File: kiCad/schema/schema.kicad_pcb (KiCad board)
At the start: 2 copper layers, 90 x 127.1 mm, 30 parts, among them J1 Conn_01x06_Pin, J11 Switch, J14 Conn_01x06_Pin, J15 MOSFET, J2 Esp32, J3 M1 Right, J4 M2 Left, J5 Bat, J6 Buck, Q1 Q_Photo_NPN, Q2 Q_Photo_NPN, Q3 Q_Photo_NPN, Q4 Q_Photo_NPN

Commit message: Day 17 - PCB 60% Done
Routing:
- net /ENC B2: track 0.00 -> 41.4 mm
- net /3V3: track 0.00 -> 37.4 mm
- net /ENC A1: track 0.00 -> 34.7 mm
- net /ENC A2: track 0.00 -> 33.2 mm, vias 0 -> 1
- net /ENC B1: track 0.00 -> 29.8 mm
- net /BIN 2: track 0.00 -> 26.6 mm, vias 0 -> 2
- net /BIN 1: track 0.00 -> 23.2 mm, vias 0 -> 2
- net /AIN 2: track 0.00 -> 19.5 mm, vias 0 -> 2
- net /AIN 1: track 0.00 -> 18.6 mm, vias 0 -> 2
- net /BUCK +: track 71.8 -> 73.0 mm
- added copper zone on B.Cu, net /GND
- added copper zone on F.Cu, net /GND

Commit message: Day 19 - PCB done
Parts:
- C1 100nF: renamed from C1
- C2 47 µF: renamed from C2
- C3 100nF: renamed from C3
- R1 120 : renamed from R1
- R10 10k: renamed from R10
- R2 120: renamed from R2
- R3 120: renamed from R3
- R4 120: renamed from R4
- R7 10k : renamed from R7
- R8 10k: renamed from R8
- R9 10k: renamed from R9
- moved C1 100nF 53.7 mm to (76.7, 108.7), turned to 90 degrees
- moved C2 47 µF 50.7 mm to (81.0, 106.7), turned to -90 degrees
- moved D3 2.85 mm to (109.9, 38.7)
- moved D4 2.14 mm to (130.1, 51.4)
- moved Q4 2.06 mm to (136.3, 57.6)
- moved R3 120 1.80 mm to (116.3, 56.6)
- moved R9 10k 1.80 mm to (121.4, 56.4)
- moved R2 120 1.27 mm to (88.4, 56.4)
- moved R8 10k 1.27 mm to (92.7, 56.6)
- moved J15 1.12 mm to (103.9, 53.1)
- moved J3 0.76 mm to (84.8, 111.5)
- moved J4 0.76 mm to (119.9, 111.5)
- moved D2 0.59 mm to (82.0, 38.7)
- moved Q3 0.31 mm to (120.3, 38.7)
- moved Q2 0.20 mm to (92.4, 38.7)
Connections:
- C1 100nF pad 1: /GND -> /BUCK +
- C1 100nF pad 2: /BUCK + -> /GND
- C2 47 µF pad 1: /BUCK + -> /GND
- C2 47 µF pad 2: /GND -> /BUCK +
- J2 pad 1: /GND -> /BUCK +
- J2 pad 13: /IR 2 -> unconnected-(J2-Pin_13-Pad13)
- J2 pad 14: /IR 1 -> unconnected-(J2-Pin_14-Pad14)
- J2 pad 18: unconnected-(J2-Pin_18-Pad18) -> /IR 1
- J2 pad 19: unconnected-(J2-Pin_19-Pad19) -> /IR 3
- J2 pad 2: /BUCK + -> /GND
- J2 pad 23: /IR 4 -> unconnected-(J2-Pin_23-Pad23)
- J2 pad 26: /IR 3 -> /IR 4
- J2 pad 27: unconnected-(J2-Pin_27-Pad27) -> /IR 2
- J2 pad 28: unconnected-(J2-Pin_28-Pad28) -> /IR EM
- J2 pad 4: /IR EM -> unconnected-(J2-Pin_4-Pad4)
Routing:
- net /BUCK +: track 73.0 -> 480.4 mm, vias 0 -> 6
- net Net-(D1-K): track 0.00 -> 111.2 mm
- net /3V3: track 37.4 -> 128.7 mm
- net /IR 1: track 0.00 -> 58.5 mm, vias 0 -> 1
- net /IR 4: track 0.00 -> 58.5 mm, vias 0 -> 1
- net /BAT +: track 13.1 -> 64.1 mm
- net /IR 3: track 0.00 -> 49.7 mm, vias 0 -> 1
- net /IR 2: track 0.00 -> 44.8 mm, vias 0 -> 1
- net Net-(J15-Pin_1): track 0.00 -> 20.2 mm
- net Net-(D4-A): track 0.00 -> 14.4 mm
- net /IR EM: track 0.00 -> 13.5 mm
- net Net-(D2-A): track 0.00 -> 11.7 mm
- net Net-(D3-A): track 0.00 -> 11.6 mm
- net Net-(D1-A): track 0.00 -> 9.62 mm
- net /AOUT 2: track 15.2 -> 13.4 mm
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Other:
- board text added: "- Isaiah 40:31"
- board text added: "Build by Serwin.dev"
- board text added: "Project ZACCH v1"
- board text added: "but those who hope in the Lord will renew their strength. They will soar on wings like eagles; they will run and not grow weary, they will walk and not be faint."

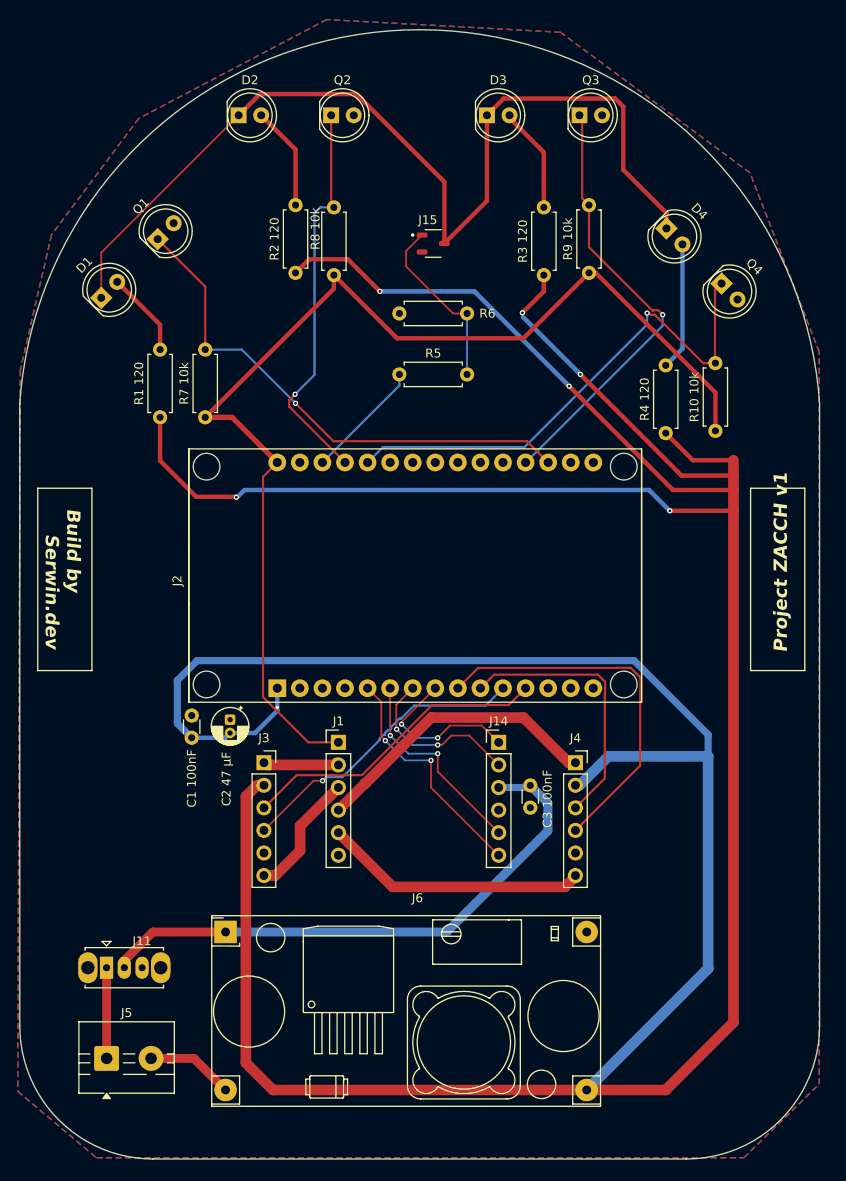
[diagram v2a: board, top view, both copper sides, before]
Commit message: Day 20 - Solved esp32 mis-pin alignment
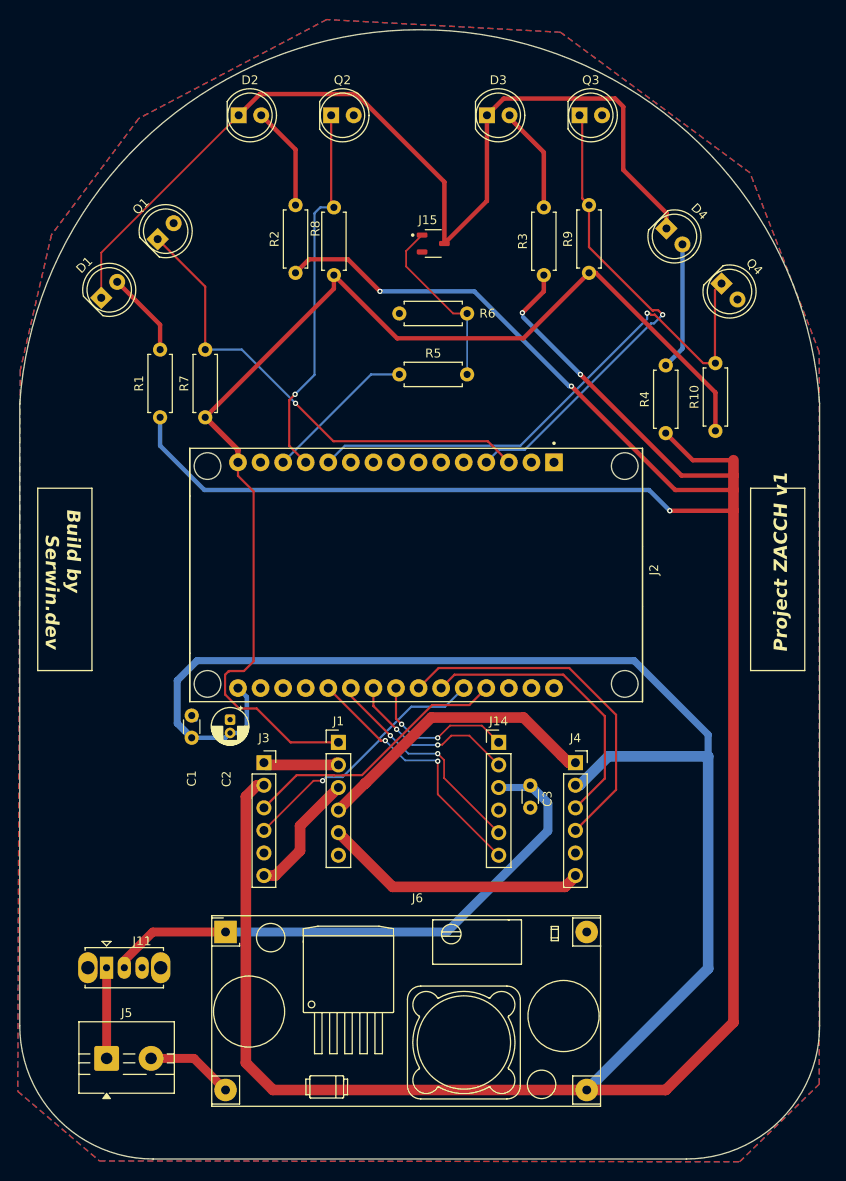
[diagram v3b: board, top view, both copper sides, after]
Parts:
- C1: renamed from C1 100nF
- C2: renamed from C2 47 µF
- C3: renamed from C3 100nF
- R1: renamed from R1 120 
- R10: renamed from R10 10k
- R2: renamed from R2 120
- R3: renamed from R3 120
- R4: renamed from R4 120
- R7: renamed from R7 10k 
- R8: renamed from R8 10k
- R9: renamed from R9 10k
- moved J2 0.11 mm to (102.0, 90.4), turned to -90 degrees
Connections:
- J2 pad 1: /BUCK + -> unconnected-(J2-Pin_1-Pad1)
- J2 pad 10: /ENC B1 -> unconnected-(J2-Pin_10-Pad10)
- J2 pad 11: /ENC A2 -> /IR 4
- J2 pad 12: /ENC A1 -> /IR 2
- J2 pad 13: unconnected-(J2-Pin_13-Pad13) -> /IR EM
- J2 pad 14: unconnected-(J2-Pin_14-Pad14) -> /GND
- J2 pad 15: unconnected-(J2-Pin_15-Pad15) -> /3V3
- J2 pad 16: unconnected-(J2-Pin_16-Pad16) -> /BUCK +
- J2 pad 17: unconnected-(J2-Pin_17-Pad17) -> /GND
- J2 pad 18: /IR 1 -> unconnected-(J2-Pin_18-Pad18)
- J2 pad 19: /IR 3 -> unconnected-(J2-Pin_19-Pad19)
- J2 pad 2: /GND -> unconnected-(J2-Pin_2-Pad2)
- J2 pad 20: unconnected-(J2-Pin_20-Pad20) -> /BIN 2
- J2 pad 21: unconnected-(J2-Pin_21-Pad21) -> /BIN 1
- J2 pad 22: unconnected-(J2-Pin_22-Pad22) -> /AIN 2
- J2 pad 23: unconnected-(J2-Pin_23-Pad23) -> /AIN 1
- J2 pad 24: unconnected-(J2-Pin_24-Pad24) -> /ENC B2
- J2 pad 25: unconnected-(J2-Pin_25-Pad25) -> /ENC B1
- J2 pad 26: /IR 4 -> /ENC A2
- J2 pad 27: /IR 2 -> /ENC A1
- J2 pad 28: /IR EM -> unconnected-(J2-Pin_28-Pad28)
- J2 pad 29: /GND -> unconnected-(J2-Pin_29-Pad29)
- J2 pad 3: unconnected-(J2-Pin_3-Pad3) -> /IR 1
- J2 pad 30: /3V3 -> unconnected-(J2-Pin_30-Pad30)
- J2 pad 4: unconnected-(J2-Pin_4-Pad4) -> /IR 3
- J2 pad 5: /BIN 2 -> unconnected-(J2-Pin_5-Pad5)
- J2 pad 6: /BIN 1 -> unconnected-(J2-Pin_6-Pad6)
- J2 pad 7: /AIN 2 -> unconnected-(J2-Pin_7-Pad7)
- J2 pad 8: /AIN 1 -> unconnected-(J2-Pin_8-Pad8)
- J2 pad 9: /ENC B2 -> unconnected-(J2-Pin_9-Pad9)
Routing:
- net /ENC A2: track 33.9 -> 29.2 mm
- net /IR 1: track 58.5 -> 54.1 mm
- net /ENC A1: track 35.0 -> 30.6 mm
- net /IR 4: track 58.5 -> 62.6 mm
- net /IR 3: track 49.7 -> 53.4 mm
- net /IR EM: track 13.5 -> 17.2 mm
- net /BUCK +: track 480.4 -> 476.8 mm, vias 6 -> 5
- net /3V3: track 128.7 -> 131.6 mm
- net /BIN 2: track 26.6 -> 29.1 mm
- net /ENC B1: track 30.6 -> 32.7 mm
- net /ENC B2: track 42.2 -> 40.2 mm
- net /BIN 1: track 23.2 -> 25.1 mm
- net /IR 2: track 44.8 -> 42.9 mm
- net /AIN 1: track 18.6 -> 17.3 mm

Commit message: Day 21 - esp32 misalignment fixed
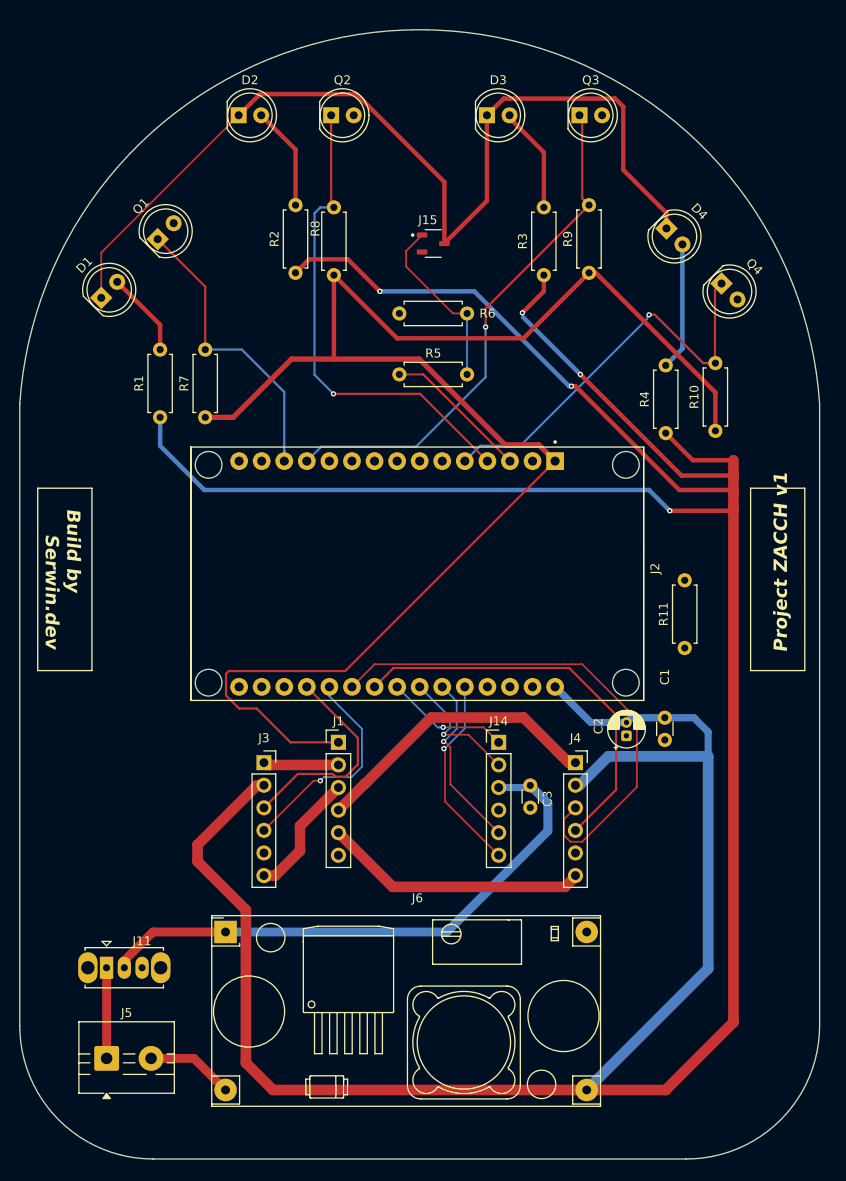
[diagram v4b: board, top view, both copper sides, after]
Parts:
- added R11: 10k ohm, Resistor_THT:R_Axial_DIN0207_L6.3mm_D2.5mm_P7.62mm_Horizontal, F.Cu at (132.2, 98.6)
- moved C1 53.3 mm to (129.9, 106.4), turned to -90 degrees
- moved C2 44.6 mm to (125.6, 108.5), turned to 90 degrees
- moved J2 1.15 mm to (102.1, 89.3), turned to 90 degrees
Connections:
- J2 pad 1: unconnected-(J2-Pin_1-Pad1) -> /3V3
- J2 pad 11: /IR 4 -> unconnected-(J2-Pin_11-Pad11)
- J2 pad 12: /IR 2 -> /IR 3
- J2 pad 13: /IR EM -> /IR 1
- J2 pad 14: /GND -> unconnected-(J2-Pin_14-Pad14)
- J2 pad 15: /3V3 -> unconnected-(J2-Pin_15-Pad15)
- J2 pad 16: /BUCK + -> unconnected-(J2-Pin_16-Pad16)
- J2 pad 17: /GND -> unconnected-(J2-Pin_17-Pad17)
- J2 pad 19: unconnected-(J2-Pin_19-Pad19) -> /ENC A1
- J2 pad 2: unconnected-(J2-Pin_2-Pad2) -> /GND
- J2 pad 20: /BIN 2 -> /ENC A2
- J2 pad 21: /BIN 1 -> /ENC B1
- J2 pad 22: /AIN 2 -> /ENC B2
- J2 pad 24: /ENC B2 -> /AIN 2
- J2 pad 25: /ENC B1 -> /BIN 1
- J2 pad 26: /ENC A2 -> /BIN 2
- J2 pad 27: /ENC A1 -> unconnected-(J2-Pin_27-Pad27)
- J2 pad 29: unconnected-(J2-Pin_29-Pad29) -> /GND
- J2 pad 3: /IR 1 -> /IR EM
- J2 pad 30: unconnected-(J2-Pin_30-Pad30) -> /BUCK +
- J2 pad 4: /IR 3 -> /IR 2
- J2 pad 5: unconnected-(J2-Pin_5-Pad5) -> /IR 4
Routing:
- net /BUCK +: track 476.8 -> 418.7 mm
- net /3V3: track 131.6 -> 179.3 mm
- net /ENC B1: track 32.7 -> 57.8 mm
- net /IR 1: track 54.1 -> 34.3 mm, vias 1 -> 0
- net /IR 4: track 62.6 -> 46.7 mm
- net /IR 2: track 42.9 -> 54.6 mm
- net /ENC A1: track 30.6 -> 24.0 mm
- net /BIN 2: track 29.1 -> 22.7 mm, vias 2 -> 1
- net /AIN 2: track 20.0 -> 14.7 mm, vias 2 -> 1
- net /IR 3: track 53.4 -> 58.7 mm
- net /BIN 1: track 25.1 -> 20.4 mm, vias 2 -> 1
- net /ENC A2: track 29.2 -> 24.5 mm
- net /ENC B2: track 40.2 -> 44.9 mm
- net /AIN 1: track 17.3 -> 14.0 mm, vias 2 -> 1
- net /IR EM: track 17.2 -> 16.5 mm
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- removed copper zone on B.Cu, net /GND
- removed copper zone on F.Cu, net /GND

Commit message: Day 22 - fix: GND error, README
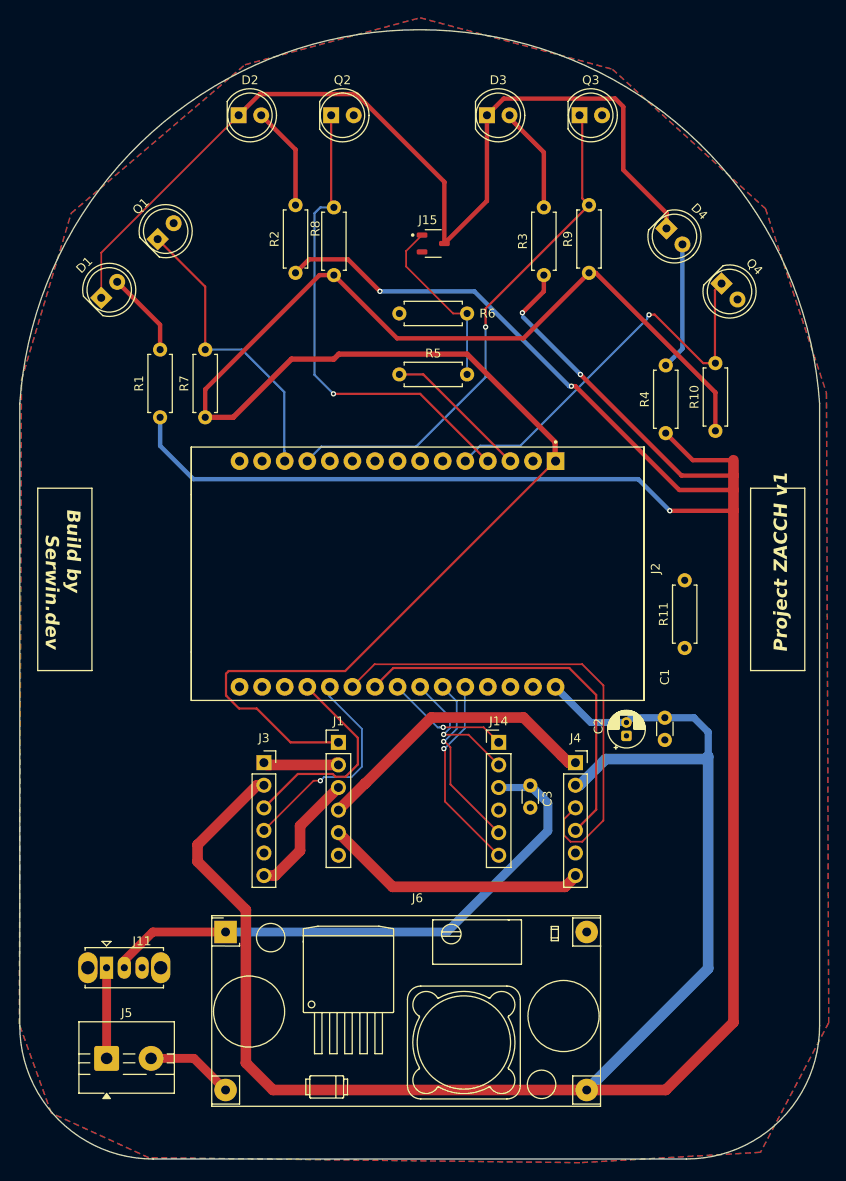
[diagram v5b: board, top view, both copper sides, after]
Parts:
- moved J2 1.00 mm to (102.1, 90.3), turned to -90 degrees
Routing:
- net /3V3: track 179.3 -> 194.5 mm
- net /ENC B1: track 57.8 -> 54.7 mm
- net /ENC B2: track 44.9 -> 43.0 mm
- added copper zone on B.Cu, net /GND
- added copper zone on F.Cu, net /GND

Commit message: Day 23: Added tactile button, boost conv
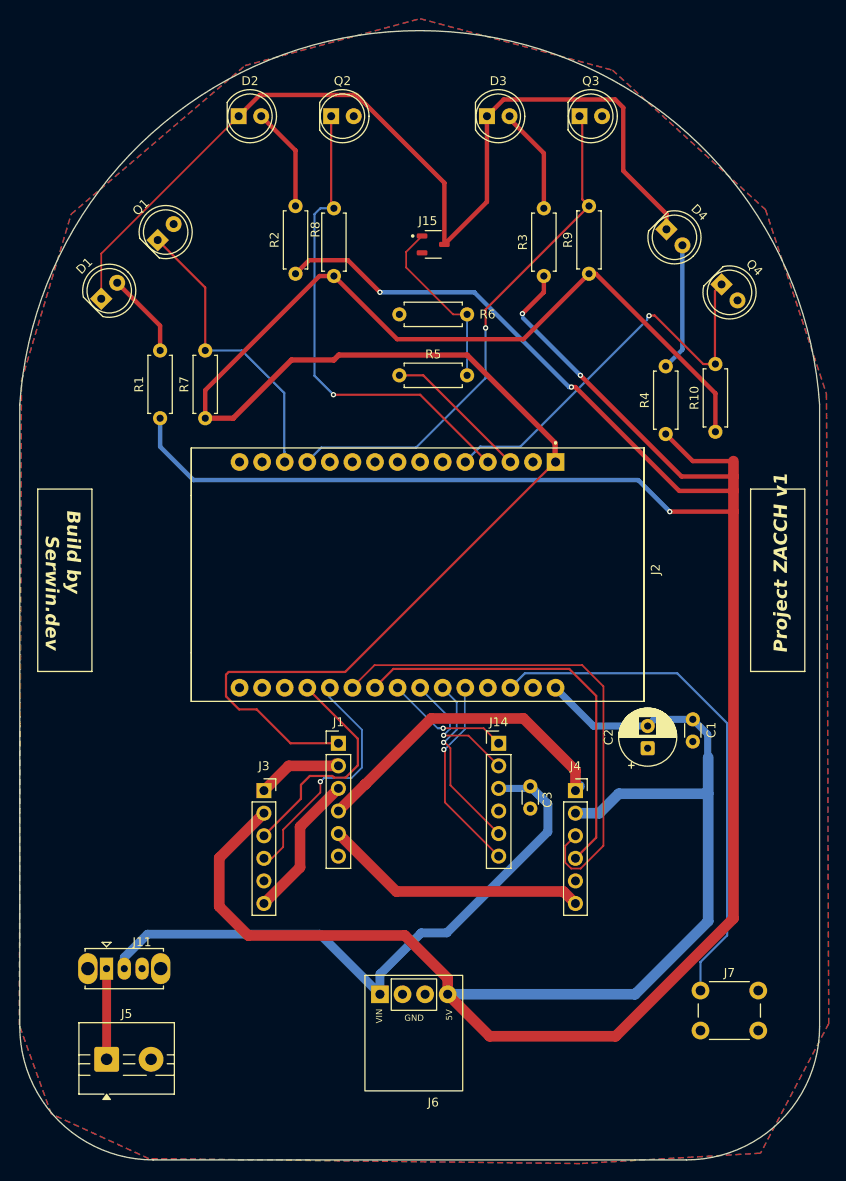
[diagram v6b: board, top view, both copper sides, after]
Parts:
- removed R11: 10k ohm, Resistor_THT:R_Axial_DIN0207_L6.3mm_D2.5mm_P7.62mm_Horizontal
- added J7: Tact Switch, Button_Switch_THT:SW_PUSH_6mm_H5mm, F.Cu at (134.0, 137.1)
- C1, C3: value C -> C 0.1
- C2: value C_Polarized -> C_Polarized 47; footprint Capacitor_THT:CP_Radial_D4.0mm_P1.50mm -> Capacitor_THT:CP_Radial_D6.3mm_P2.50mm
- J6: value Buck -> BOOST; footprint footprints:YAAJ_DCDC_StepDown_LM2596 -> footprints:TPS61023
- moved J6 24.0 mm to (101.7, 141.9)
- moved C1 3.15 mm to (133.1, 106.6)
- moved J3 3.14 mm to (84.8, 114.7)
- moved J4 3.14 mm to (119.9, 114.7)
- moved C2 2.77 mm to (128.0, 109.9)
- moved D4 0.10 mm to (130.1, 51.5)
- moved J1 0.10 mm to (93.2, 109.3)
- moved J14 0.10 mm to (111.3, 109.3)
- moved J15 0.10 mm to (103.9, 53.2)
- moved R2 0.10 mm to (88.4, 56.5)
- moved R4 0.10 mm to (130.0, 74.5)
- moved R5 0.10 mm to (100.1, 67.9)
- moved R9 0.10 mm to (121.4, 56.5)
- moved D1 0.10 mm to (66.5, 59.3)
- moved D2 0.10 mm to (82.0, 38.8)
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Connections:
- C1 pad 1: /BUCK + -> /BOOST +
- C2 pad 2: /BUCK + -> /BOOST +
- J2 pad 28: unconnected-(J2-Pin_28-Pad28) -> /SW PIN
- J2 pad 30: /BUCK + -> /BOOST +
- J3 pad 2: /BUCK + -> /BOOST +
- J4 pad 2: /BUCK + -> /BOOST +
- J6 pad 3: /BUCK + -> /GND
- J6 pad 4: /GND -> /BOOST +
- R1 pad 1: /BUCK + -> /BOOST +
- R2 pad 1: /BUCK + -> /BOOST +
- R3 pad 1: /BUCK + -> /BOOST +
- R4 pad 1: /BUCK + -> /BOOST +
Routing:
- net /BUCK +: track 418.7 -> 0.00 mm, vias 5 -> 0
- net /BOOST +: track 0.00 -> 401.2 mm, vias 0 -> 5
- net /SW PIN: track 0.00 -> 58.7 mm
- net /GND: track 9.88 -> 0.02 mm
- net /BAT +: track 64.1 -> 71.3 mm
- net /ENC A2: track 24.5 -> 27.6 mm
- net /AOUT 2: track 13.4 -> 16.4 mm
- net /BOUT 1: track 33.1 -> 36.1 mm
- net /ENC B2: track 43.0 -> 46.1 mm
- net /ENC B1: track 54.7 -> 57.2 mm
- net /ENC A1: track 24.0 -> 26.0 mm
- net /AOUT 1: track 8.85 -> 9.90 mm

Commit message: Day 24 -- Final commit on V1
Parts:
- added Motor mount: MountingHole_3.2mm_M3, MountingHole:MountingHole_3.2mm_M3, F.Cu at (129.8, 121.0)
- added Motor mount: MountingHole_3.2mm_M3, MountingHole:MountingHole_3.2mm_M3, F.Cu at (75.0, 121.0)
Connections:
- C3 pad 1: /GND -> /BAT +
- C3 pad 2: /BAT + -> /GND
- J14 pad 3: /BAT + -> /GND
- J14 pad 4: /GND -> /BAT +
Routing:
- net /BAT +: track 71.3 -> 68.7 mm

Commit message: Fix: Organized Schematic folder
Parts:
- Boost conv: renamed from J6
- J1: value Conn_01x06_Pin -> DRV8833
- J14: value Conn_01x06_Pin -> GND
- Motor A: renamed from J4
- Motor B: renamed from J3
- Tact Switch: renamed from J7
- renumbered J5 to Battery, J2 to Esp32, J11 to Switch
